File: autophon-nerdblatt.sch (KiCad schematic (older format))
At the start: 20 parts, among them J1 board-edge-connector

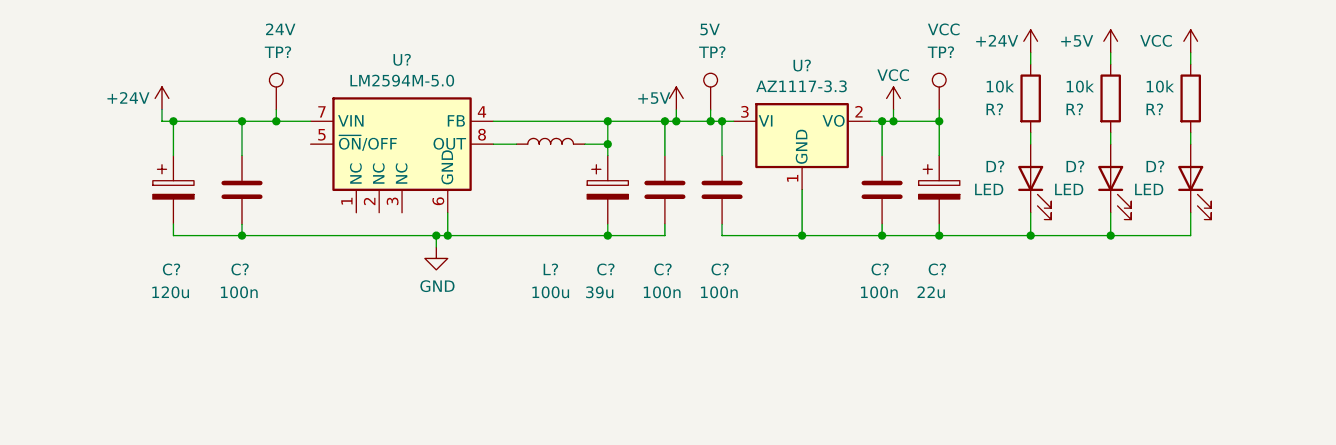
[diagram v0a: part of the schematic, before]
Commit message: Added footprints.
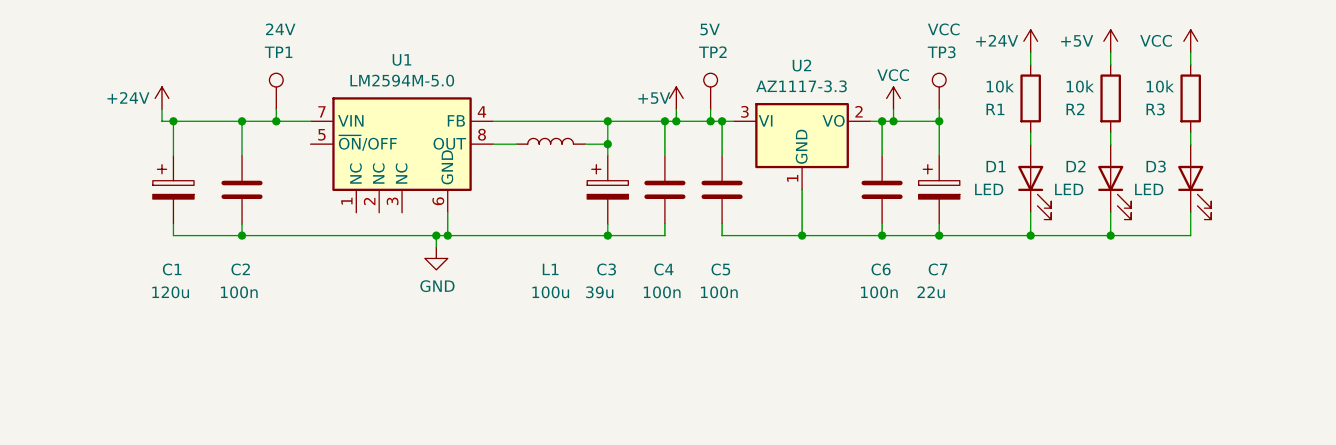
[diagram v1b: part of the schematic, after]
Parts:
- C1, C3, C7: renamed from C?; footprint (none) -> Capacitor_SMD:CP_Elec_6.3x7.7
- C2, C4, C5, C6: renamed from C?; footprint (none) -> Capacitor_SMD:C_0603_1608Metric
- D1, D2, D3: renamed from D?; footprint (none) -> LED_SMD:LED_0603_1608Metric
- L1: renamed from L?; footprint (none) -> Inductor_SMD:L_1812_4532Metric_Pad1.30x3.40mm_HandSolder
- R1, R2, R3: renamed from R?; footprint (none) -> Resistor_SMD:R_0603_1608Metric
- TP1, TP2, TP3: renamed from TP?; footprint (none) -> TestPoint:TestPoint_Pad_1.5x1.5mm
- U2: renamed from U?; footprint (none) -> Package_TO_SOT_SMD:SOT-223-3_TabPin2
- gave numbers to parts that had none: 1
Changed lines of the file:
@@
 P 7050 1100
 AR Path="/5FCC89CF/6024443E" Ref="U?"  Part="1"
-AR Path="/6024443E" Ref="U?"  Part="1"
-F 0 "U?" H 7050 1467 50  0000 C CNN
+AR Path="/6024443E" Ref="U1"  Part="1"
+F 0 "U1" H 7050 1467 50  0000 C CNN
 F 1 "LM2594M-5.0" H 7050 1376 50  0000 C CNN
 F 2 "Package_SO:SOIC-8_3.9x4.9mm_P1.27mm" H 7250 850 50  0001 L CIN
@@
 P 6350 1300
 AR Path="/5FCC89CF/60244444" Ref="C?"  Part="1"
-AR Path="/60244444" Ref="C?"  Part="1"
-F 0 "C?" H 6300 950 50  0000 L CNN
+AR Path="/60244444" Ref="C2"  Part="1"
+F 0 "C2" H 6300 950 50  0000 L CNN
 F 1 "100n" H 6250 850 50  0000 L CNN
-F 2 "" H 6388 1150 50  0001 C CNN
+F 2 "Capacitor_SMD:C_0603_1608Metric" H 6388 1150 50  0001 C CNN
 F 3 "~" H 6350 1300 50  0001 C CNN
 	1    6350 1300
@@
 P 6050 1300
 AR Path="/5FCC89CF/6024444A" Ref="C?"  Part="1"
-AR Path="/6024444A" Ref="C?"  Part="1"
-F 0 "C?" H 6000 950 50  0000 L CNN
+AR Path="/6024444A" Ref="C1"  Part="1"
+F 0 "C1" H 6000 950 50  0000 L CNN
 F 1 "120u" H 5950 850 50  0000 L CNN
-F 2 "" H 6088 1150 50  0001 C CNN
+F 2 "Capacitor_SMD:CP_Elec_6.3x7.7" H 6088 1150 50  0001 C CNN
 F 3 "~" H 6050 1300 50  0001 C CNN
 	1    6050 1300
@@
 AR Path="/5FC6F066/6024445B" Ref="#PWR?"  Part="1"
 AR Path="/5FCC89CF/6024445B" Ref="#PWR?"  Part="1"
-AR Path="/6024445B" Ref="#PWR?"  Part="1"
-F 0 "#PWR?" H 6000 800 50  0001 C CNN
+AR Path="/6024445B" Ref="#PWR0101"  Part="1"
+F 0 "#PWR0101" H 6000 800 50  0001 C CNN
 F 1 "+24V" H 5850 1000 50  0000 C CNN
 F 2 "" H 6000 950 50  0001 C CNN
@@
 AR Path="/5FC6F066/60244464" Ref="#PWR?"  Part="1"
 AR Path="/5FCC89CF/60244464" Ref="#PWR?"  Part="1"
-AR Path="/60244464" Ref="#PWR?"  Part="1"
-F 0 "#PWR?" H 8250 800 50  0001 C CNN
+AR Path="/60244464" Ref="#PWR0102"  Part="1"
+F 0 "#PWR0102" H 8250 800 50  0001 C CNN
 F 1 "+5V" H 8150 1000 50  0000 C CNN
 F 2 "" H 8250 950 50  0001 C CNN
@@
 P 7700 1100
 AR Path="/5FCC89CF/6024446A" Ref="L?"  Part="1"
-AR Path="/6024446A" Ref="L?"  Part="1"
-F 0 "L?" V 7150 1100 50  0000 C CNN
+AR Path="/6024446A" Ref="L1"  Part="1"
+F 0 "L1" V 7150 1100 50  0000 C CNN
 F 1 "100u" V 7050 1100 50  0000 C CNN
-F 2 "" H 7700 1100 50  0001 C CNN
+F 2 "Inductor_SMD:L_1812_4532Metric_Pad1.30x3.40mm_HandSolder" H 7700 1100 50  0001 C CNN
 F 3 "~" H 7700 1100 50  0001 C CNN
 	1    7700 1100
@@
 P 7950 1300
 AR Path="/5FCC89CF/60244470" Ref="C?"  Part="1"
-AR Path="/60244470" Ref="C?"  Part="1"
-F 0 "C?" H 7900 950 50  0000 L CNN
+AR Path="/60244470" Ref="C3"  Part="1"
+F 0 "C3" H 7900 950 50  0000 L CNN
 F 1 "39u" H 7850 850 50  0000 L CNN
-F 2 "" H 7988 1150 50  0001 C CNN
+F 2 "Capacitor_SMD:CP_Elec_6.3x7.7" H 7988 1150 50  0001 C CNN
 F 3 "~" H 7950 1300 50  0001 C CNN
 	1    7950 1300
@@
 P 8200 1300
 AR Path="/5FCC89CF/60244476" Ref="C?"  Part="1"
-AR Path="/60244476" Ref="C?"  Part="1"
-F 0 "C?" H 8150 950 50  0000 L CNN
+AR Path="/60244476" Ref="C4"  Part="1"
+F 0 "C4" H 8150 950 50  0000 L CNN
 F 1 "100n" H 8100 850 50  0000 L CNN
-F 2 "" H 8238 1150 50  0001 C CNN
+F 2 "Capacitor_SMD:C_0603_1608Metric" H 8238 1150 50  0001 C CNN
 F 3 "~" H 8200 1300 50  0001 C CNN
 	1    8200 1300
@@
 P 8800 1000
 AR Path="/5FC6F066/60254C9D" Ref="U?"  Part="1"
-AR Path="/60254C9D" Ref="U?"  Part="1"
-F 0 "U?" H 8800 1242 50  0000 C CNN
+AR Path="/60254C9D" Ref="U2"  Part="1"
+F 0 "U2" H 8800 1242 50  0000 C CNN
 F 1 "AZ1117-3.3" H 8800 1151 50  0000 C CNN
-F 2 "" H 8800 1250 50  0001 C CIN
+F 2 "Package_TO_SOT_SMD:SOT-223-3_TabPin2" H 8800 1250 50  0001 C CIN
 F 3 "https://www.diodes.com/assets/Datasheets/AZ1117.pdf" H 8800 1000 50  0001 C CNN
 	1    8800 1000
@@
 P 9200 950
 AR Path="/5FC6F066/60254CA9" Ref="#PWR?"  Part="1"
-AR Path="/60254CA9" Ref="#PWR?"  Part="1"
-F 0 "#PWR?" H 9200 800 50  0001 C CNN
+AR Path="/60254CA9" Ref="#PWR0103"  Part="1"
+F 0 "#PWR0103" H 9200 800 50  0001 C CNN
 F 1 "VCC" H 9200 1100 50  0000 C CNN
 F 2 "" H 9200 950 50  0001 C CNN
@@
 P 8450 1300
 AR Path="/5FCC89CF/60255E36" Ref="C?"  Part="1"
-AR Path="/60255E36" Ref="C?"  Part="1"
-F 0 "C?" H 8400 950 50  0000 L CNN
+AR Path="/60255E36" Ref="C5"  Part="1"
+F 0 "C5" H 8400 950 50  0000 L CNN
 F 1 "100n" H 8350 850 50  0000 L CNN
-F 2 "" H 8488 1150 50  0001 C CNN
+F 2 "Capacitor_SMD:C_0603_1608Metric" H 8488 1150 50  0001 C CNN
 F 3 "~" H 8450 1300 50  0001 C CNN
 	1    8450 1300
@@
 $EndComp
 $Comp
-L Device:LED D?
+L Device:LED D1
 U 1 1 60258CE7
 P 9800 1250
-F 0 "D?" V 9850 1450 50  0000 R CNN
+F 0 "D1" V 9850 1450 50  0000 R CNN
 F 1 "LED" V 9750 1500 50  0000 R CNN
-F 2 "" H 9800 1250 50  0001 C CNN
+F 2 "LED_SMD:LED_0603_1608Metric" H 9800 1250 50  0001 C CNN
 F 3 "~" H 9800 1250 50  0001 C CNN
 	1    9800 1250
@@
 AR Path="/5FC6F066/6025B863" Ref="#PWR?"  Part="1"
 AR Path="/5FCC89CF/6025B863" Ref="#PWR?"  Part="1"
-AR Path="/6025B863" Ref="#PWR?"  Part="1"
-F 0 "#PWR?" H 9800 550 50  0001 C CNN
+AR Path="/6025B863" Ref="#PWR0104"  Part="1"
+F 0 "#PWR0104" H 9800 550 50  0001 C CNN
 F 1 "+24V" H 9650 750 50  0000 C CNN
 F 2 "" H 9800 700 50  0001 C CNN
@@
 $EndComp
 $Comp
-L Device:R R?
+L Device:R R1
 U 1 1 6025E2B0
 P 9800 900
-F 0 "R?" H 9600 850 50  0000 L CNN
+F 0 "R1" H 9600 850 50  0000 L CNN
 F 1 "10k" H 9600 950 50  0000 L CNN
-F 2 "" V 9730 900 50  0001 C CNN
+F 2 "Resistor_SMD:R_0603_1608Metric" V 9730 900 50  0001 C CNN
 F 3 "~" H 9800 900 50  0001 C CNN
 	1    9800 900
@@
 	9800 1050 9800 1100
 $Comp
-L power:GND #PWR?
+L power:GND #PWR0105
 U 1 1 602626B3
 P 7200 1550
-F 0 "#PWR?" H 7200 1300 50  0001 C CNN
+F 0 "#PWR0105" H 7200 1300 50  0001 C CNN
 F 1 "GND" H 7205 1377 50  0000 C CNN
 F 2 "" H 7200 1550 50  0001 C CNN
@@
 P 9150 1300
 AR Path="/5FCC89CF/60268173" Ref="C?"  Part="1"
-AR Path="/60268173" Ref="C?"  Part="1"
-F 0 "C?" H 9100 950 50  0000 L CNN
+AR Path="/60268173" Ref="C6"  Part="1"
+F 0 "C6" H 9100 950 50  0000 L CNN
 F 1 "100n" H 9050 850 50  0000 L CNN
-F 2 "" H 9188 1150 50  0001 C CNN
+F 2 "Capacitor_SMD:C_0603_1608Metric" H 9188 1150 50  0001 C CNN
 F 3 "~" H 9150 1300 50  0001 C CNN
 	1    9150 1300
@@
 P 9400 1300
 AR Path="/5FCC89CF/6026B486" Ref="C?"  Part="1"
-AR Path="/6026B486" Ref="C?"  Part="1"
-F 0 "C?" H 9350 950 50  0000 L CNN
+AR Path="/6026B486" Ref="C7"  Part="1"
+F 0 "C7" H 9350 950 50  0000 L CNN
 F 1 "22u" H 9300 850 50  0000 L CNN
-F 2 "" H 9438 1150 50  0001 C CNN
+F 2 "Capacitor_SMD:CP_Elec_6.3x7.7" H 9438 1150 50  0001 C CNN
 F 3 "~" H 9400 1300 50  0001 C CNN
 	1    9400 1300
@@
 	9150 1000 9200 1000
 $Comp
-L Device:LED D?
+L Device:LED D2
 U 1 1 60274C8D
 P 10150 1250
-F 0 "D?" V 10200 1450 50  0000 R CNN
+F 0 "D2" V 10200 1450 50  0000 R CNN
 F 1 "LED" V 10100 1500 50  0000 R CNN
-F 2 "" H 10150 1250 50  0001 C CNN
+F 2 "LED_SMD:LED_0603_1608Metric" H 10150 1250 50  0001 C CNN
 F 3 "~" H 10150 1250 50  0001 C CNN
 	1    10150 1250
@@
 $EndComp
 $Comp
-L Device:R R?
+L Device:R R2
 U 1 1 60274DE9
 P 10150 900
-F 0 "R?" H 9950 850 50  0000 L CNN
+F 0 "R2" H 9950 850 50  0000 L CNN
 F 1 "10k" H 9950 950 50  0000 L CNN
-F 2 "" V 10080 900 50  0001 C CNN
+F 2 "Resistor_SMD:R_0603_1608Metric" V 10080 900 50  0001 C CNN
 F 3 "~" H 10150 900 50  0001 C CNN
 	1    10150 900
@@
 	10150 1050 10150 1100
 $Comp
-L Device:LED D?
+L Device:LED D3
 U 1 1 60283430
 P 10500 1250
-F 0 "D?" V 10550 1450 50  0000 R CNN
+F 0 "D3" V 10550 1450 50  0000 R CNN
 F 1 "LED" V 10450 1500 50  0000 R CNN
-F 2 "" H 10500 1250 50  0001 C CNN
+F 2 "LED_SMD:LED_0603_1608Metric" H 10500 1250 50  0001 C CNN
 F 3 "~" H 10500 1250 50  0001 C CNN
 	1    10500 1250
@@
 $EndComp
 $Comp
-L Device:R R?
+L Device:R R3
 U 1 1 602835BC
 P 10500 900
-F 0 "R?" H 10300 850 50  0000 L CNN
+F 0 "R3" H 10300 850 50  0000 L CNN
 F 1 "10k" H 10300 950 50  0000 L CNN
-F 2 "" V 10430 900 50  0001 C CNN
+F 2 "Resistor_SMD:R_0603_1608Metric" V 10430 900 50  0001 C CNN
 F 3 "~" H 10500 900 50  0001 C CNN
 	1    10500 900
@@
 P 10500 700
 AR Path="/5FC6F066/60292C1D" Ref="#PWR?"  Part="1"
-AR Path="/60292C1D" Ref="#PWR?"  Part="1"
-F 0 "#PWR?" H 10500 550 50  0001 C CNN
+AR Path="/60292C1D" Ref="#PWR0106"  Part="1"
+F 0 "#PWR0106" H 10500 550 50  0001 C CNN
 F 1 "VCC" H 10350 750 50  0000 C CNN
 F 2 "" H 10500 700 50  0001 C CNN
@@
 AR Path="/5FC6F066/60292FDB" Ref="#PWR?"  Part="1"
 AR Path="/5FCC89CF/60292FDB" Ref="#PWR?"  Part="1"
-AR Path="/60292FDB" Ref="#PWR?"  Part="1"
-F 0 "#PWR?" H 10150 550 50  0001 C CNN
+AR Path="/60292FDB" Ref="#PWR0107"  Part="1"
+F 0 "#PWR0107" H 10150 550 50  0001 C CNN
 F 1 "+5V" H 10000 750 50  0000 C CNN
 F 2 "" H 10150 700 50  0001 C CNN
@@
 $EndComp
 $Comp
-L Connector:TestPoint TP?
+L Connector:TestPoint TP3
 U 1 1 60294D1C
 P 9400 950
-F 0 "TP?" H 9350 1200 50  0000 L CNN
+F 0 "TP3" H 9350 1200 50  0000 L CNN
 F 1 "VCC" H 9350 1300 50  0000 L CNN
-F 2 "" H 9600 950 50  0001 C CNN
+F 2 "TestPoint:TestPoint_Pad_1.5x1.5mm" H 9600 950 50  0001 C CNN
 F 3 "~" H 9600 950 50  0001 C CNN
 	1    9400 950
@@
 Connection ~ 9400 1000
 $Comp
-L Connector:TestPoint TP?
+L Connector:TestPoint TP2
 U 1 1 602A3AFA
 P 8400 950
-F 0 "TP?" H 8350 1200 50  0000 L CNN
+F 0 "TP2" H 8350 1200 50  0000 L CNN
 F 1 "5V" H 8350 1300 50  0000 L CNN
-F 2 "" H 8600 950 50  0001 C CNN
+F 2 "TestPoint:TestPoint_Pad_1.5x1.5mm" H 8600 950 50  0001 C CNN
 F 3 "~" H 8600 950 50  0001 C CNN
 	1    8400 950
@@
 	8400 1000 8450 1000
 $Comp
-L Connector:TestPoint TP?
+L Connector:TestPoint TP1
 U 1 1 602A508A
 P 6500 950
-F 0 "TP?" H 6450 1200 50  0000 L CNN
+F 0 "TP1" H 6450 1200 50  0000 L CNN
 F 1 "24V" H 6450 1300 50  0000 L CNN
-F 2 "" H 6700 950 50  0001 C CNN
+F 2 "TestPoint:TestPoint_Pad_1.5x1.5mm" H 6700 950 50  0001 C CNN
 F 3 "~" H 6700 950 50  0001 C CNN
 	1    6500 950

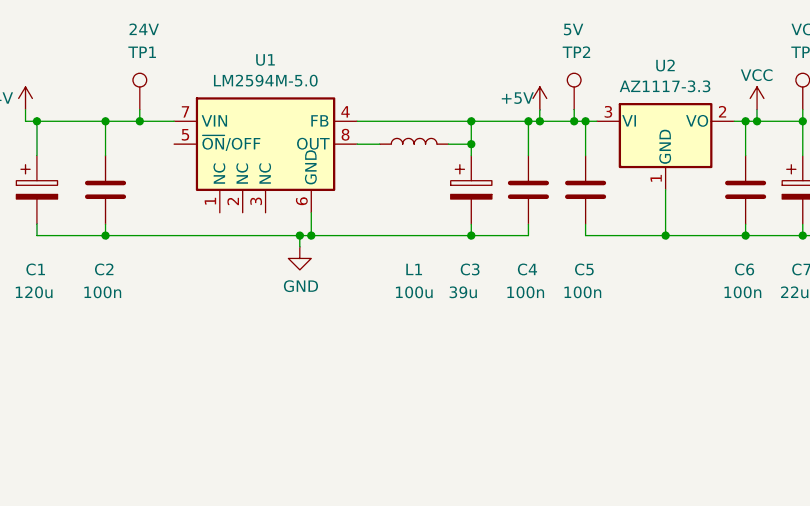
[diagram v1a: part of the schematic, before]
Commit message: caps for long high impedance traces. distributor info.
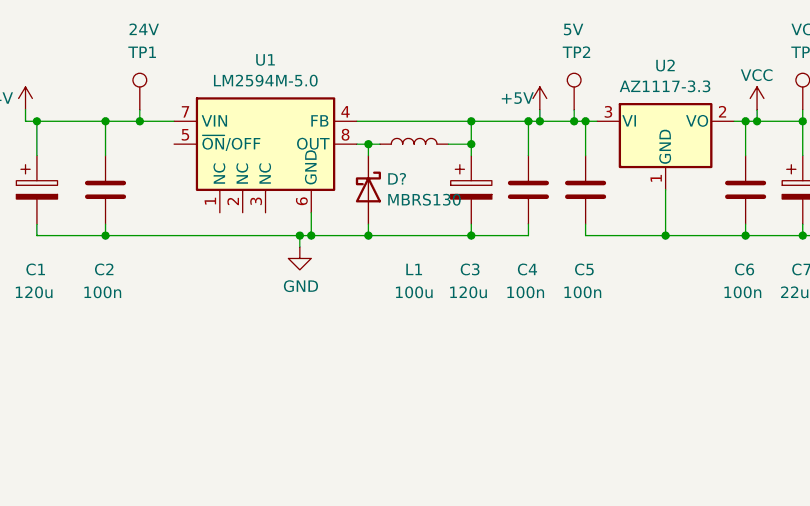
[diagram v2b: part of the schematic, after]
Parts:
- added D?: MBRS130, symbol Device:D_Schottky
- C3: value 39u -> 120u
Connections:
- net GND: now also D?.2 (A)
- net at L1.1, U1.8 (OUT): now also D?.1 (K)
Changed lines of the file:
@@
 AR Path="/60244470" Ref="C3"  Part="1"
 F 0 "C3" H 7900 950 50  0000 L CNN
-F 1 "39u" H 7850 850 50  0000 L CNN
+F 1 "120u" H 7850 850 50  0000 L CNN
 F 2 "Capacitor_SMD:CP_Elec_6.3x7.7" H 7988 1150 50  0001 C CNN
 F 3 "~" H 7950 1300 50  0001 C CNN
@@
 	7950 1000 8200 1000
 Wire Wire Line
-	7250 1500 7950 1500
+	7250 1500 7500 1500
 Wire Wire Line
 	8200 1500 8200 1450
@@
 	7950 1500 8200 1500
 Wire Wire Line
-	7450 1100 7550 1100
+	7450 1100 7500 1100
 Wire Wire Line
 	7850 1100 7950 1100
@@
 Text Notes 9050 6300 0    50   ~ 0
 (only global labels)
+$Comp
+L Device:D_Schottky D?
+U 1 1 5FCB94B0
+P 7500 1300
+F 0 "D?" V 7454 1380 50  0000 L CNN
+F 1 "MBRS130" V 7545 1380 50  0000 L CNN
+F 2 "" H 7500 1300 50  0001 C CNN
+F 3 "~" H 7500 1300 50  0001 C CNN
+F 4 "Reichelt" H 7500 1300 50  0001 C CNN "Distri"
+F 5 "https://www.reichelt.de/schottky-barrier-gleichrichter-30v-1-0-a-do-214aa-smb-mbrs-130lt3g-ons-p219508.html?search=MBRS130" H 7500 1300 50  0001 C CNN "Link"
+	1    7500 1300
+	0    1    1    0
+$EndComp
+Wire Wire Line
+	7500 1100 7500 1150
+Connection ~ 7500 1100
+Wire Wire Line
+	7500 1100 7550 1100
+Wire Wire Line
+	7500 1450 7500 1500
+Connection ~ 7500 1500
+Wire Wire Line
+	7500 1500 7950 1500
 $EndSCHEMATC
